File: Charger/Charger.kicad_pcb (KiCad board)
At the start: 2 copper layers, 168 parts, among them J1 Bat_ballanser_conn, J2 Battery_conn, J3 Power_conn, J4 Screen_SPInCtrlnPwr_Conn, J5 User_Interface_Conn, J6 1/0_Select_Conn, J8 Temp_Sens_Conn, Q1 BC846BW, Q10 MJD45H11T4, Q11 MJD45H11T4, Q12 MJD45H11T4, Q13 BC846BW, Q14 MJD31CT4, Q15 BUJ302AD, Q16 BUJ302AD, Q17 IRF7404, Q18 IRF7404, Q19 BC846BW, Q2 BC846BW, Q3 BC846BW, Q4 MJD45H11T4, Q5 MJD45H11T4, Q6 MJD45H11T4, Q7 BC846BW, Q8 BC846BW, Q9 BC846BW, U1 LM2904, U10 MCP6001-OT, U12 ACS712xLCTR-20A, U13 MCP6004, U17 XL4015, U18 XL4015, U19 MCP6001-OT, U2 LM2904, U20 LM2575-12BU, U21 L7805, U22 LDI1117-3.3, U23 RaspberryPi_Pico, U24 CD4051B, U25 MCP6004, U3 LM2904, U4 LM2904, U5 LM2904, U6 LM2904

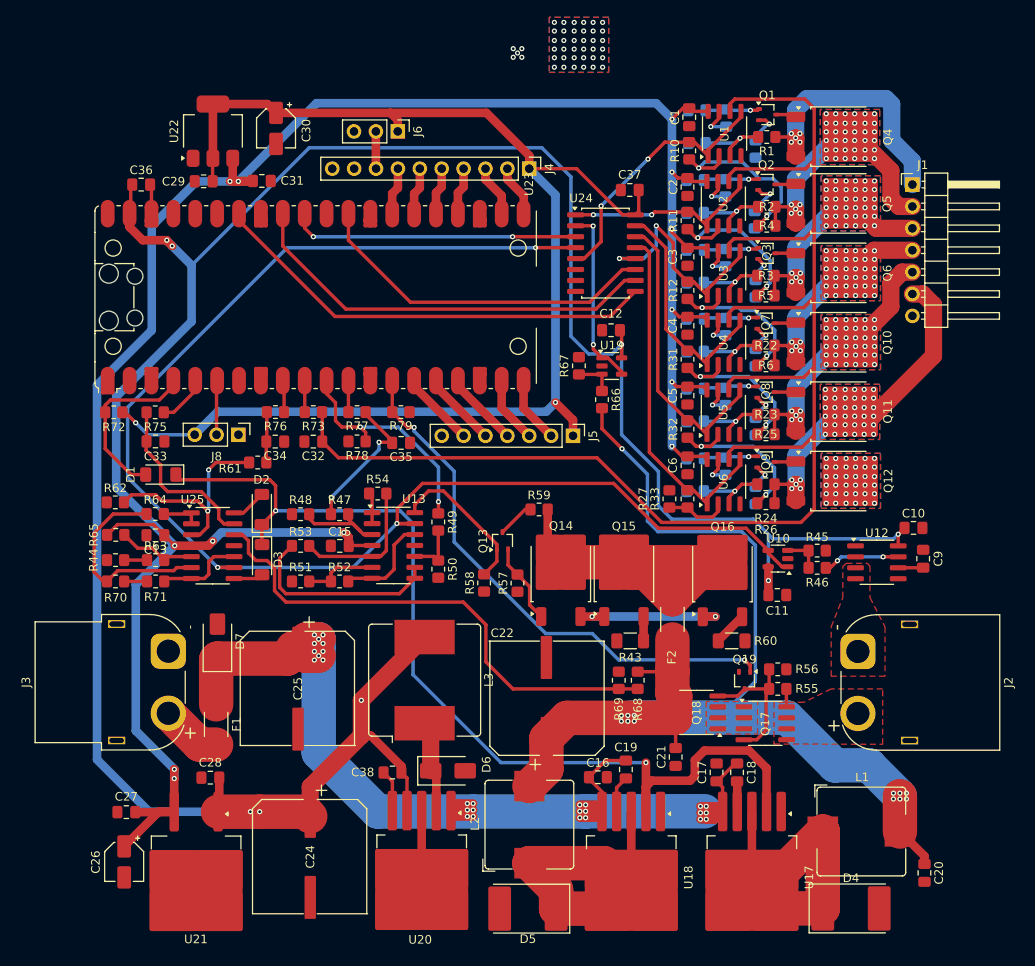
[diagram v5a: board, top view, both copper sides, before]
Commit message: PCB V1
do przerobienia jedynie numery elementów na wartości jedno i drugi w miare poukladane tylko podmienic i posprawdzać
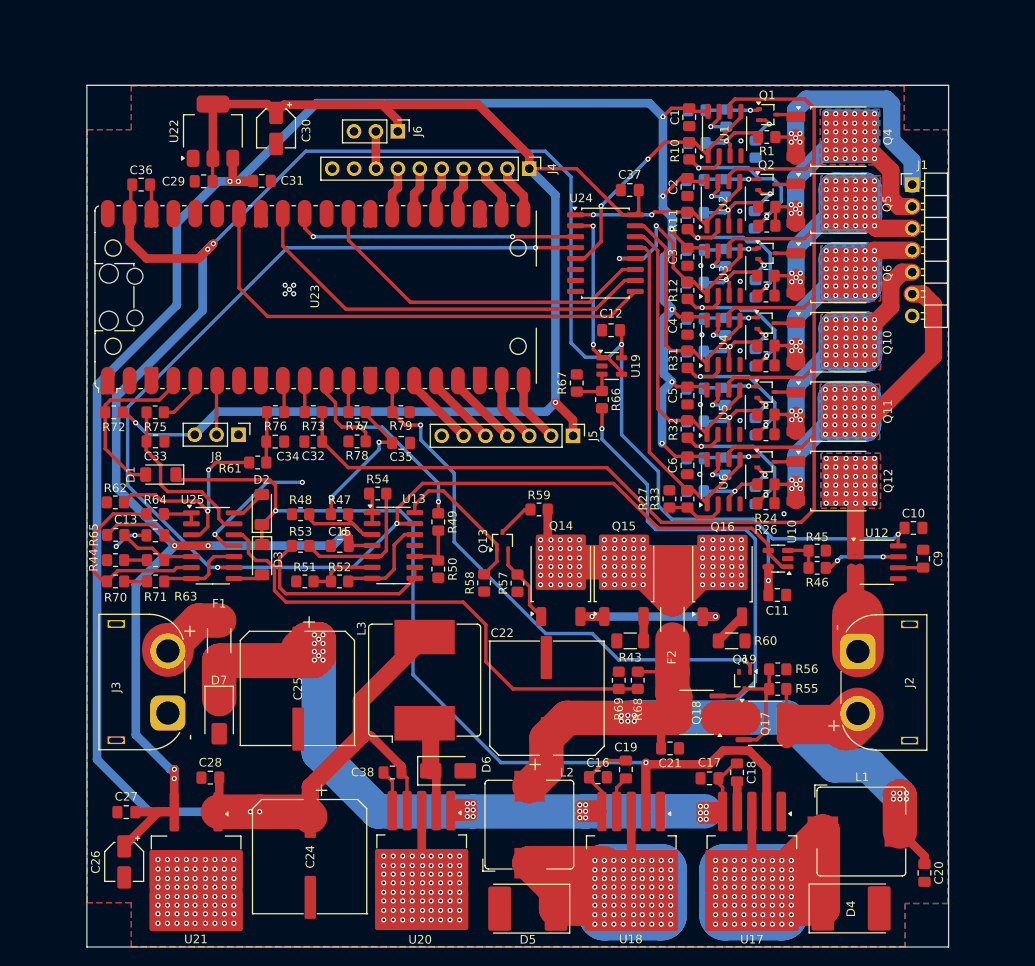
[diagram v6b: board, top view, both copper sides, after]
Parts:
- J3: footprint Connector_AMASS:AMASS_XT60PW-F_1x02_P7.20mm_Horizontal -> Connector_AMASS:AMASS_XT60PW-M_1x02_P7.20mm_Horizontal
- U10: value MCP6001-OT -> MCP6001
- moved F1 9.73 mm to (108.3, 109.3), turned to -90 degrees
- moved D7 8.72 mm to (108.3, 118.2), turned to -90 degrees
- moved J3 7.18 mm to (102.4, 117.8)
- moved R67 2.02 mm to (149.8, 79.5)
- moved C21 1.19 mm to (160.7, 121.8), turned to 0 degrees
- moved C17 1.07 mm to (165.2, 125.3), turned to 180 degrees
- moved R51 0.50 mm to (118.3, 102.5)
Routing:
- net /Sztuczne_obciazenie/B+: track 38.2 -> 124.2 mm, vias 0 -> 90
- net /Pomiar pradu/BAT+: track 2.10 -> 41.2 mm
- net /Balanser/B5: track 26.6 -> 61.8 mm
- net GND: track 18.2 -> 48.0 mm, vias 36 -> 199
- net Net-(D4-K): track 38.2 -> 62.8 mm, vias 0 -> 72
- net Net-(D5-K): track 38.4 -> 62.5 mm, vias 0 -> 72
- net /Pomiar pradu/BAT-: track 0.00 -> 19.0 mm
- net +36V: track 123.9 -> 136.9 mm
- net /Balanser/B1: track 36.3 -> 49.3 mm
- net /Balanser/B3: track 22.3 -> 35.2 mm
- net /Balanser/B2: track 26.2 -> 39.2 mm
- net /Balanser/B4: track 22.8 -> 34.7 mm
- net GPIO28: track 51.8 -> 56.4 mm
- net +5V: track 279.0 -> 282.8 mm
- net +12V: track 279.8 -> 283.4 mm, vias 11 -> 10
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- removed copper zone on B.Cu, net (none)
- removed copper zone on F.Cu, net (none)
- removed copper zone on F.Cu, net /Pomiar pradu/BAT+
- removed copper zone on F.Cu, net /Pomiar pradu/BAT-
- removed copper zone on F.Cu, net Net-(Q17-S-Pad1)
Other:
- board outline added: 100 x 100 mm

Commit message: pcb gotowe do sprawdzenia
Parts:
- added *CHARGER_EN: TestPoint_Pad_D1.0mm, TestPoint:TestPoint_Pad_D1.0mm, B.Cu at (110.6, 82.8)
- added ADC: TestPoint_Pad_D1.0mm, TestPoint:TestPoint_Pad_D1.0mm, B.Cu at (118.3, 59.7)
- added BALL_SET_V: TestPoint_Pad_D1.0mm, TestPoint:TestPoint_Pad_D1.0mm, B.Cu at (119.8, 82.8)
- added BATTERY_EN: TestPoint_Pad_D1.0mm, TestPoint:TestPoint_Pad_D1.0mm, B.Cu at (128.4, 82.8)
- added CHARGER_SET_I: TestPoint_Pad_D1.0mm, TestPoint:TestPoint_Pad_D1.0mm, B.Cu at (117.0, 82.9)
- added CHARGER_SET_V: TestPoint_Pad_D1.0mm, TestPoint:TestPoint_Pad_D1.0mm, B.Cu at (113.8, 82.8)
- added HALL: TestPoint_Pad_D1.0mm, TestPoint:TestPoint_Pad_D1.0mm, B.Cu at (144.0, 66.6)
- added HALL: TestPoint_Pad_D1.0mm, TestPoint:TestPoint_Pad_D1.0mm, B.Cu at (177.7, 100.3)
- added LOAD_EN: TestPoint_Pad_D1.0mm, TestPoint:TestPoint_Pad_D1.0mm, B.Cu at (125.6, 82.8)
- added LOAD_SET_I: TestPoint_Pad_D1.0mm, TestPoint:TestPoint_Pad_D1.0mm, B.Cu at (122.7, 82.8)
- added REF**: MountingHole_2.2mm_M2, MountingHole:MountingHole_2.2mm_M2, F.Cu at (190.5, 47.4)
- added REF**: MountingHole_2.2mm_M2, MountingHole:MountingHole_2.2mm_M2, F.Cu at (95.5, 142.4)
- added REF**: MountingHole_2.2mm_M2, MountingHole:MountingHole_2.2mm_M2, F.Cu at (95.5, 47.4)
- added REF**: MountingHole_2.2mm_M2, MountingHole:MountingHole_2.2mm_M2, F.Cu at (190.5, 142.4)
- added VB1: TestPoint_Pad_D1.0mm, TestPoint:TestPoint_Pad_D1.0mm, B.Cu at (156.4, 66.3)
- added VB2: TestPoint_Pad_D1.0mm, TestPoint:TestPoint_Pad_D1.0mm, B.Cu at (153.6, 66.3)
- added VB3: TestPoint_Pad_D1.0mm, TestPoint:TestPoint_Pad_D1.0mm, B.Cu at (156.4, 63.7)
- added VB4: TestPoint_Pad_D1.0mm, TestPoint:TestPoint_Pad_D1.0mm, B.Cu at (153.6, 63.7)
- added VB5: TestPoint_Pad_D1.0mm, TestPoint:TestPoint_Pad_D1.0mm, B.Cu at (156.4, 61.6)
- added VB6: TestPoint_Pad_D1.0mm, TestPoint:TestPoint_Pad_D1.0mm, B.Cu at (153.6, 61.6)
- added VOUT: TestPoint_Pad_D1.0mm, TestPoint:TestPoint_Pad_D1.0mm, B.Cu at (153.6, 69.5)
- added VOUT: TestPoint_Pad_D1.0mm, TestPoint:TestPoint_Pad_D1.0mm, B.Cu at (150.8, 118.5)
- F2: value Fuse_Small -> 10A
- Q19: value BC846BW -> BC846
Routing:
- net GPIO2: track 21.2 -> 42.3 mm, vias 0 -> 1
- net /Ladowarka/Set V: track 20.1 -> 37.2 mm, vias 0 -> 1
- net +3.3V: track 157.9 -> 165.7 mm
- net /Balanser/V_bat_2: track 35.3 -> 42.9 mm, vias 0 -> 1
- net /MCU/LOAD_SetI: track 17.1 -> 23.4 mm
- net /Ladowarka/Vout: track 144.2 -> 148.5 mm
- net GPIO10: track 64.6 -> 68.5 mm
- net /Ladowarka/Set I: track 6.06 -> 9.84 mm, vias 0 -> 1
- net /Ladowarka/Hall: track 164.9 -> 168.2 mm
- net ADC_0: track 32.7 -> 35.9 mm
- net /Balanser/V_bat_5: track 22.8 -> 25.6 mm
- net /Balanser/V_bat_3: track 28.4 -> 31.0 mm, vias 0 -> 1
- net Net-(U12-VIOUT): track 8.93 -> 11.4 mm
- net /Balanser/V_bat_1: track 41.0 -> 43.1 mm, vias 0 -> 1
- net GPIO8: track 26.3 -> 28.4 mm
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
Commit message: Changed SPI connector and MUX pins
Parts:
- removed J6: 1/0_Select_Conn, Connector_PinHeader_2.54mm:PinHeader_1x03_P2.54mm_Vertical
- F2: value 10A -> Fuse_Small
- Q19: value BC846 -> BC846BW
- U10: value MCP6001 -> MCP6001-OT
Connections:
- J4 pad 8: /MCU/SPI_BL -> GPIO22
- U23 pad 7: unconnected-(U23-GPIO5-Pad7) -> GPIO5
- U24 pad 10: GPIO27 -> GPIO28
- U24 pad 11: GPIO22 -> GPIO27
- U24 pad 9: GPIO28 -> GPIO5
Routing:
- net GPIO5: track 0.00 -> 50.7 mm
- net GPIO22: track 40.6 -> 7.35 mm
- net /MCU/SPI_BL: track 4.33 -> 0.00 mm
- net +3.3V: track 165.7 -> 161.8 mm
- net GPIO28: track 56.4 -> 57.2 mm
- net GPIO27: track 48.3 -> 48.8 mm
